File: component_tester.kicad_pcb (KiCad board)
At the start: 2 copper layers, 93 x 34 mm, 77 parts, among them IC1 ATMEGA16U2, IC2 ATMEGA328P-A, P1 USB_OTG, P10 BO_PC5, P11 ICSP_prog_328p, P12 BO_PD2, P13 BO_PD3, P14 BO_PD4, P15 BO_PD5, P16 BO_PD6, P17 CONN_01X01, P18 Device Under Test, P2 BATTERY_CONNECTOR, P3 Voltage_for_zener, P4 ICSP_prog_16u2, P5 BO_PC7, P6 BO_PD0, P7 BO_PD1, P8 BO_PC4, P9 BO_PC6, Q1 TRANSISTOR_NPN_2N2222_KSP222A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, SW1 ON-OFF switch, SW2 DO_MEASUREMENT, SW3 CONNECT_CAP, U1 NCP1117ST50T3G, U2 XF2L-2625-1A, U3 LT1004, U4 CDSOT23-SRV05-4, Y1 8MHz, Y2 16MHz

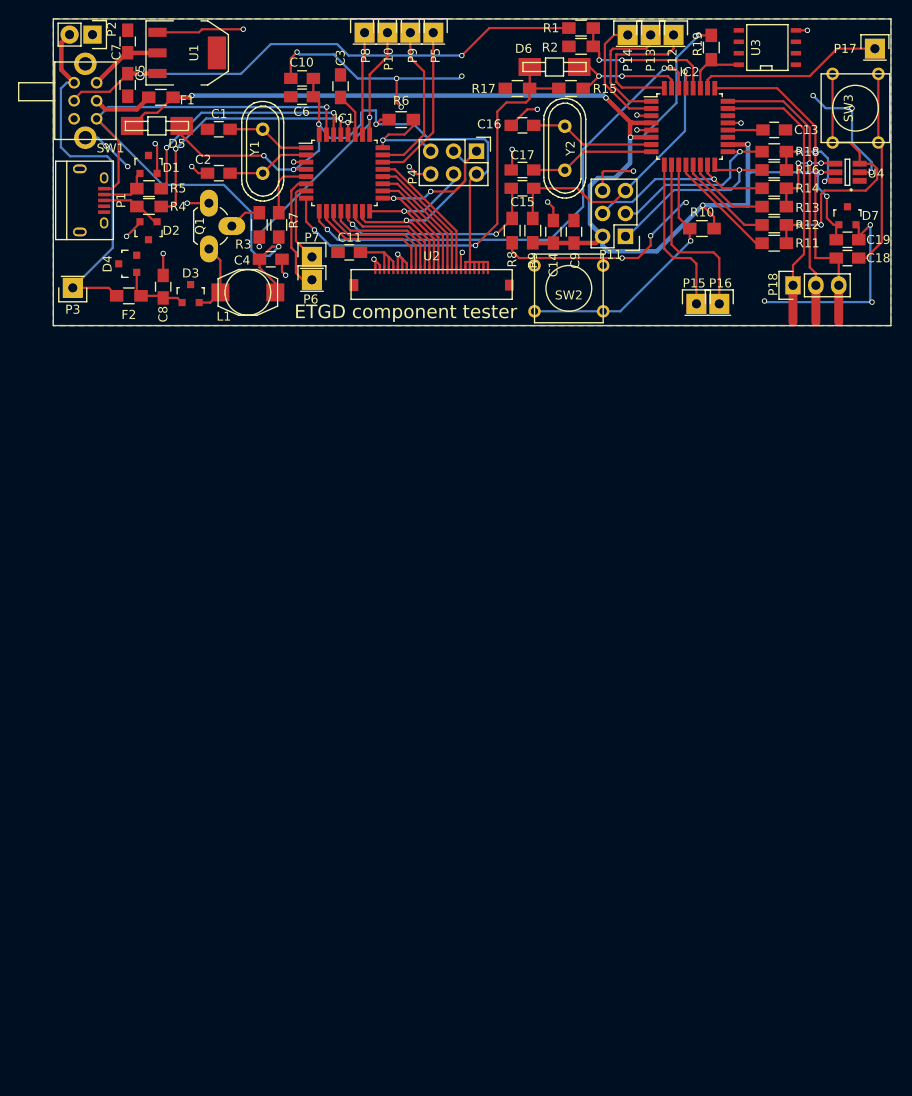
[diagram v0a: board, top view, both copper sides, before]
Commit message: Updated schematic. New PCB layout.
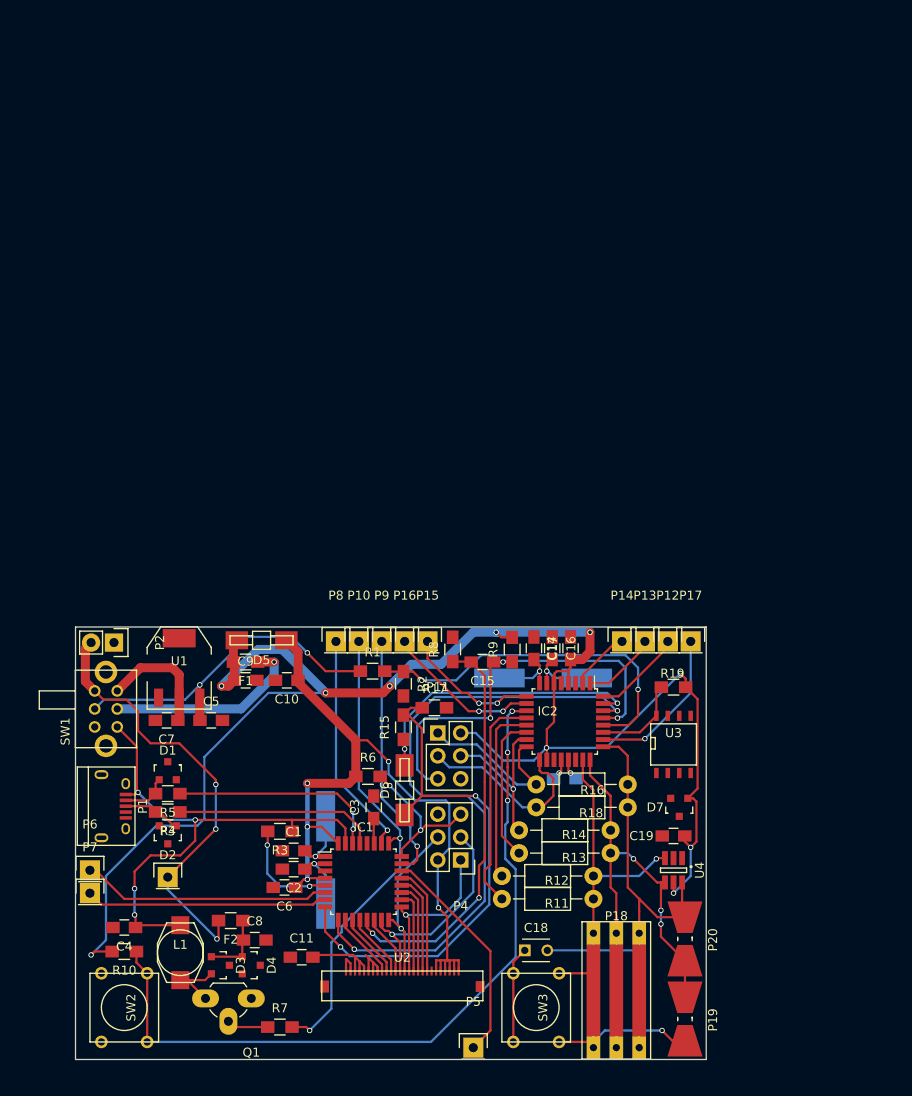
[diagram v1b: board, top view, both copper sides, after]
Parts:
- added P19: DUT_SMD_1_2, Resistors_Universal:Resistor_SMDuniversal_0805to2512_HandSoldering, F.Cu at (167.6, 143.5)
- added P20: DUT_SMD_2_3, Resistors_Universal:Resistor_SMDuniversal_0805to2512_HandSoldering, F.Cu at (167.6, 134.6)
- C13: moved to B.Cu
- C18: footprint Capacitors_SMD:C_0805_HandSoldering -> Capacitors_ThroughHole:C_Disc_D3_P2.5
- P18: footprint Pin_Headers:Pin_Header_Straight_1x03 -> drawn_by_jpmeijers:CONN_DUT
- R11, R12, R13, R14, R16, R18: footprint Resistors_SMD:R_0805_HandSoldering -> Resistors_ThroughHole:Resistor_Horizontal_RM10mm
- Y1, Y2: footprint Crystals:Crystal_HC49-U_Vertical -> Crystals:Crystal_HC49-SD_SMD; moved to B.Cu
- moved P5 112.7 mm to (144.1, 146.7)
- moved SW3 105.9 mm to (151.1, 142.2), turned to 270 degrees
- moved R10 102.7 mm to (105.4, 136.0), turned to 180 degrees
- moved SW2 93.8 mm to (105.4, 142.2), turned to 270 degrees
- moved R7 89.1 mm to (122.7, 144.4), turned to 0 degrees
- moved Q1 88.4 mm to (119.5, 141.2), turned to 180 degrees
- moved C6 87.8 mm to (123.2, 128.9)
- moved C18 84.8 mm to (149.9, 135.9), turned to 0 degrees
- moved D6 82.0 mm to (136.5, 118.1), turned to 270 degrees
- moved C1 80.5 mm to (124.2, 124.8)
- moved C3 80.1 mm to (133.1, 120.0)
- moved U4 79.8 mm to (166.4, 127.0), turned to 270 degrees
- moved D4 79.1 mm to (119.5, 137.5), turned to 270 degrees
- moved Y1 79.0 mm to (127.8, 125.9)
- moved IC1 78.7 mm to (132.0, 128.3)
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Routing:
- net GND: track 156.2 -> 10.3 mm, vias 36 -> 1
- net Net-(IC2-Pad11): track 29.7 -> 85.0 mm, vias 1 -> 3
- net 5Volt_328: track 154.2 -> 183.4 mm, vias 8 -> 10
- net /Battery_measure: track 17.0 -> 40.2 mm
- net Batt_Switch: track 61.5 -> 38.3 mm
- net Net-(C15-Pad2): track 24.2 -> 45.1 mm
- net /CHARGER_SWITCHING: track 32.7 -> 52.8 mm
- net UART_16u_TO_328: track 55.4 -> 73.4 mm
- net Net-(D6-Pad2): track 14.1 -> 32.0 mm
- net Net-(IC1-Pad7): track 9.07 -> 26.9 mm
- net /USB_Vcc: track 76.7 -> 59.1 mm, vias 2 -> 4
- net Net-(F1-Pad1): track 6.73 -> 22.3 mm, vias 0 -> 1
- net Net-(IC1-Pad6): track 13.4 -> 27.7 mm
- net /RESET_328: track 32.2 -> 46.4 mm, vias 1 -> 3
- net Net-(IC1-Pad26): track 11.4 -> 25.1 mm, vias 0 -> 1
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- removed copper zone on B.Cu, net GND
- removed copper zone on F.Cu, net GND
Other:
- board size 93 x 34 mm -> 70 x 48 mm
- rule pad_to_mask_clearance: 0.2 -> 0
- board text removed: "2016-06-17"
- board text removed: "ETGD component tester"

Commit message: Version 3 of the PCB
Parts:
- added C12: 1n, Capacitors_SMD:C_0805_HandSoldering, B.Cu at (150.7, 124.6)
- added P21: ICSP_prog_328_4, Pin_Headers:Pin_Header_Straight_1x01, F.Cu at (142.2, 119.4)
- added P22: ICSP_prog_328_5, Pin_Headers:Pin_Header_Straight_1x01, F.Cu at (160.0, 116.8)
- added P23: CONN_01X01, Pin_Headers:Pin_Header_Straight_1x01, F.Cu at (161.3, 120.3)
- added P24: Device Under Test, drawn_by_jpmeijers:CONN_DUT, F.Cu at (149.8, 135.2)
- added P25: CONN_01X03, drawn_by_jpmeijers:CONN_DUT_SMD, F.Cu at (165.9, 143.8)
- C1, C16, C19, C2, C3, C5, C6, C7, R10, U4: moved to B.Cu
- C13: value 1n -> 100n
- C15: value 100n -> 22pF; moved to B.Cu
- C17: value 22pF -> 22nF high quality; footprint Capacitors_SMD:C_0805_HandSoldering -> Capacitors_ThroughHole:C_Disc_D3_P2.5
- C18: value 22nF high quality -> 100n; footprint Capacitors_ThroughHole:C_Disc_D3_P2.5 -> Capacitors_SMD:C_0805_HandSoldering
- P10: value BO_PC5 -> ICSP_prog_16u2_4
- P11: value ICSP_prog_328p -> BO_PC6; footprint Pin_Headers:Pin_Header_Straight_2x03 -> Pin_Headers:Pin_Header_Straight_1x01
- P12: value BO_PD2 -> ICSP_prog_16u2_5
- P13: value BO_PD3 -> BO_PC5
- P14: value BO_PD4 -> BO_PD2
- P15: value BO_PD5 -> BO_PD3
- P16: value BO_PD6 -> BO_PD4
- P17: value CONN_01X01 -> BO_PD5
- P18: value Device Under Test -> BO_PD6; footprint drawn_by_jpmeijers:CONN_DUT -> Pin_Headers:Pin_Header_Straight_1x01
- P19: value DUT_SMD_1_2 -> ICSP_prog_328_1; footprint Resistors_Universal:Resistor_SMDuniversal_0805to2512_HandSoldering -> Pin_Headers:Pin_Header_Straight_1x01
- P20: value DUT_SMD_2_3 -> ICSP_prog_328_3; footprint Resistors_Universal:Resistor_SMDuniversal_0805to2512_HandSoldering -> Pin_Headers:Pin_Header_Straight_1x01
- P4: value ICSP_prog_16u2 -> BO_PC7; footprint Pin_Headers:Pin_Header_Straight_2x03 -> Pin_Headers:Pin_Header_Straight_1x01
- P5: value BO_PC7 -> ICSP_prog_16u2_1
- P9: value BO_PC6 -> ICSP_prog_16u2_3
- Q1: footprint TO_SOT_Packages_THT:TO-92_Rugged -> TO_SOT_Packages_THT:TO-92_Inline_Narrow_Oval
- R1: value 100k -> R
- R11, R12, R13, R14, R16, R18: footprint Resistors_ThroughHole:Resistor_Horizontal_RM10mm -> Resistors_SMD:R_0805_HandSoldering
- R2: value 33k -> 22
- R3: value R -> 22
- R4: value 22 -> 10k
- R5: value 22 -> 100k
- R6: value 10k -> 33k
- U2: footprint drawn_by_jpmeijers:XF2L-2625-1A -> drawn_by_jpmeijers:CONN_FPC_FFC_0.5mm_26PIN_DRAWER_BOTTOM
- Y1, Y2: footprint Crystals:Crystal_HC49-SD_SMD -> Crystals:Crystal_HC49-U_Vertical; moved to F.Cu
- moved R10 47.0 mm to (148.0, 116.1), turned to 0 degrees
- moved C17 45.2 mm to (140.7, 146.4), turned to 0 degrees
- moved P10 36.3 mm to (135.3, 137.7)
- moved P9 36.1 mm to (132.7, 137.7)
- moved P19 33.3 mm to (142.2, 121.9), turned to 0 degrees
- moved P12 31.9 mm to (135.6, 112.3)
- moved R2 31.7 mm to (109.9, 123.6), turned to 180 degrees
- moved F2 31.7 mm to (102.4, 104.6)
- moved P13 31.3 mm to (132.8, 109.3)
- moved R5 31.1 mm to (138.3, 105.1), turned to 0 degrees
- moved R15 30.4 mm to (166.8, 112.9)
- moved D6 29.1 mm to (165.0, 112.0), turned to 90 degrees
- moved P17 28.4 mm to (142.2, 113.0)
- moved P20 26.9 mm to (142.2, 126.0), turned to 0 degrees
- moved P18 25.6 mm to (142.2, 115.6)
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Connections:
- C13 pad 1: Net-(C13-Pad1) -> 5Volt_328
- C14 pad 1: 5Volt_328 -> /RESET_328
- C14 pad 2: GND -> Net-(C14-Pad2)
- C15 pad 1: /RESET_328 -> GND
- C17 pad 1: GND -> Net-(C17-Pad1)
- C17 pad 2: Net-(C17-Pad2) -> /DUT3
- C18 pad 1: Net-(C18-Pad1) -> 5Volt_328
- C18 pad 2: /DUT3 -> GND
- C8 pad 1: Net-(C8-Pad1) -> Battery_fused
- D3 pad 1: Net-(C8-Pad1) -> Battery_fused
- D4 pad 1: Net-(C8-Pad1) -> Battery_fused
- F1 pad 2: 5Volt_328 -> /USB_Vcc
- F2 pad 1: Net-(C8-Pad1) -> Battery_input
- F2 pad 2: Battery_input -> Battery_fused
- IC1 pad 13: Net-(C15-Pad2) -> Net-(C14-Pad2)
- IC2 pad 15: Net-(IC2-Pad15) -> /328_MOSI
- IC2 pad 16: Net-(IC2-Pad16) -> /328_MISO
- IC2 pad 17: Net-(IC2-Pad17) -> /328_SCK
- IC2 pad 20: Net-(C13-Pad1) -> Net-(C12-Pad1)
- IC2 pad 7: Net-(C16-Pad2) -> Net-(C15-Pad2)
- IC2 pad 8: Net-(C17-Pad2) -> Net-(C16-Pad2)
- P1 pad 1: /USB_Vcc -> Net-(F1-Pad1)
- P10 pad 1: /CHARGER_SWITCHING -> /LCD_DATA_B2
- P11 pad 1: Net-(IC2-Pad16) -> Net-(IC1-Pad23)
- P12 pad 1: Net-(IC2-Pad32) -> /RESET_16u
- P13 pad 1: Net-(IC2-Pad1) -> /CHARGER_SWITCHING
- P14 pad 1: Net-(IC2-Pad2) -> Net-(IC2-Pad32)
- P15 pad 1: Net-(IC2-Pad9) -> Net-(IC2-Pad1)
- P16 pad 1: Net-(IC2-Pad10) -> Net-(IC2-Pad2)
- P17 pad 1: Net-(IC2-Pad26) -> Net-(IC2-Pad9)
- P18 pad 1: /DUT1 -> Net-(IC2-Pad10)
- P19 pad 1: /DUT2 -> /328_MISO
- P20 pad 1: /DUT3 -> /328_SCK
- P3 pad 1: Battery_input -> Battery_fused
- P4 pad 1: /LCD_DATA_B3 -> Net-(IC1-Pad22)
- P5 pad 1: Net-(IC1-Pad22) -> /LCD_DATA_B3
- P9 pad 1: Net-(IC1-Pad23) -> /LCD_DATA_B1
- R1 pad 1: Batt_Switch -> /USB_Vcc
- R1 pad 2: /Battery_measure -> /CHARGER_VOLTAGE_SENSE
- R14 pad 2: Net-(IC2-Pad15) -> /328_MOSI
- R16 pad 2: Net-(IC2-Pad16) -> /328_MISO
- R18 pad 2: Net-(IC2-Pad17) -> /328_SCK
- R2 pad 1: /Battery_measure -> Net-(IC1-Pad29)
- R2 pad 2: GND -> /USB_D+
- R3 pad 1: /USB_Vcc -> Net-(IC1-Pad30)
- R3 pad 2: /CHARGER_VOLTAGE_SENSE -> /USB_D-
- R4 pad 1: Net-(IC1-Pad29) -> 3Volt_16u
- R4 pad 2: /USB_D+ -> /RESET_16u
- R5 pad 1: Net-(IC1-Pad30) -> Batt_Switch
- R5 pad 2: /USB_D- -> /Battery_measure
- R6 pad 1: 3Volt_16u -> /Battery_measure
- R6 pad 2: /RESET_16u -> GND
- R8 pad 1: Net-(C15-Pad2) -> Net-(C14-Pad2)
- SW1 pad 1: Net-(F1-Pad1) -> 5Volt_328
- SW1 pad 5: Battery_input -> Battery_fused
- SW3 pad 2: Net-(C18-Pad1) -> Net-(C17-Pad1)
- Y2 pad 1: Net-(C16-Pad2) -> Net-(C15-Pad2)
- Y2 pad 2: Net-(C17-Pad2) -> Net-(C16-Pad2)
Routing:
- net Battery_fused: track 0.00 -> 47.4 mm
- net Battery_input: track 49.1 -> 3.06 mm, vias 3 -> 0
- net Net-(C14-Pad2): track 0.00 -> 43.9 mm, vias 0 -> 2
- net Net-(C15-Pad2): track 45.1 -> 6.25 mm, vias 2 -> 0
- net /RESET_328: track 46.4 -> 10.9 mm, vias 3 -> 0
- net UART_16u_TO_328: track 73.4 -> 41.9 mm
- net Net-(IC1-Pad23): track 27.8 -> 3.94 mm, vias 1 -> 0
- net /Reference_voltage: track 10.1 -> 32.8 mm
- net Net-(IC1-Pad22): track 25.1 -> 2.77 mm
- net /CHARGER_SWITCHING: track 52.8 -> 31.3 mm
- net Net-(IC1-Pad6): track 27.7 -> 6.36 mm
- net Net-(IC2-Pad17): track 20.7 -> 0.00 mm
- net Net-(D6-Pad2): track 32.0 -> 11.6 mm, vias 2 -> 0
- net Net-(IC2-Pad16): track 18.9 -> 0.00 mm
- net Net-(IC2-Pad15): track 18.8 -> 0.00 mm, vias 1 -> 0
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- added copper zone on B.Cu, net GND
- added copper zone on F.Cu, net GND

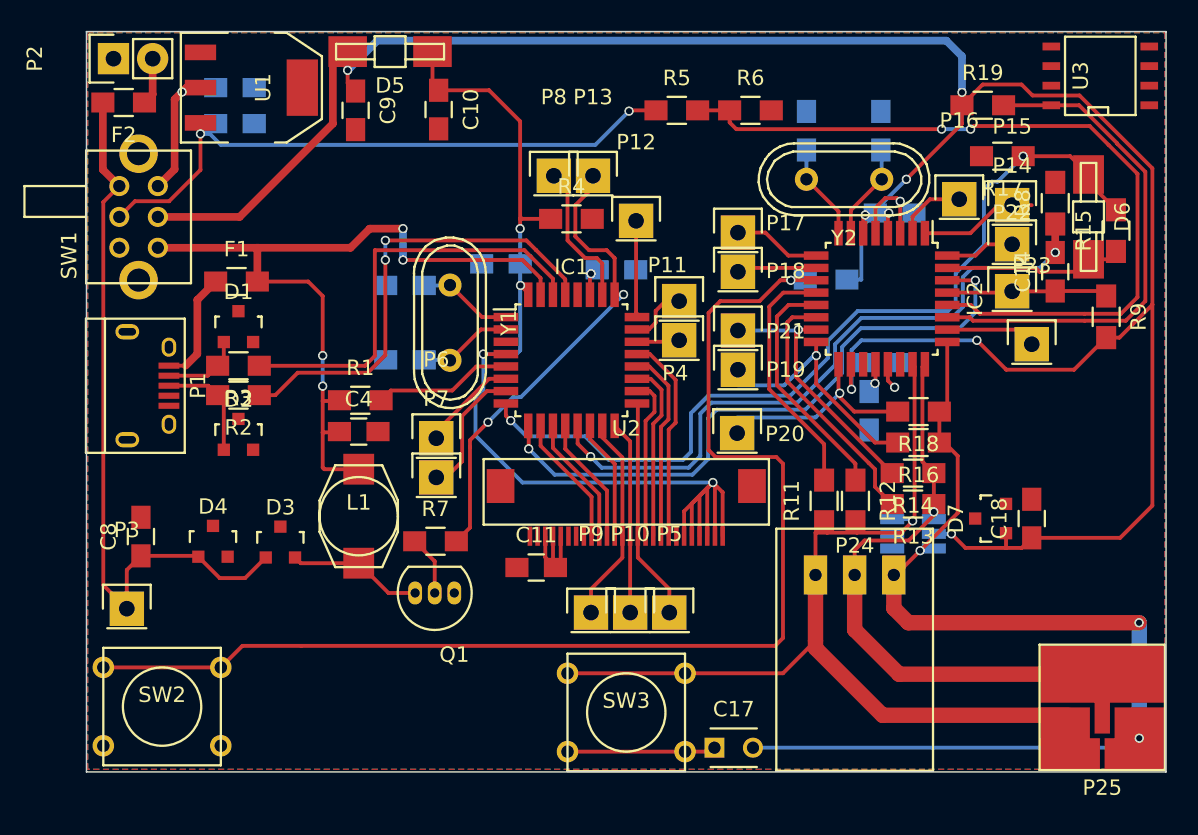
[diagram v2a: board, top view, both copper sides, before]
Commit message: Resonator Capacitor closer. A lot of GND vias.
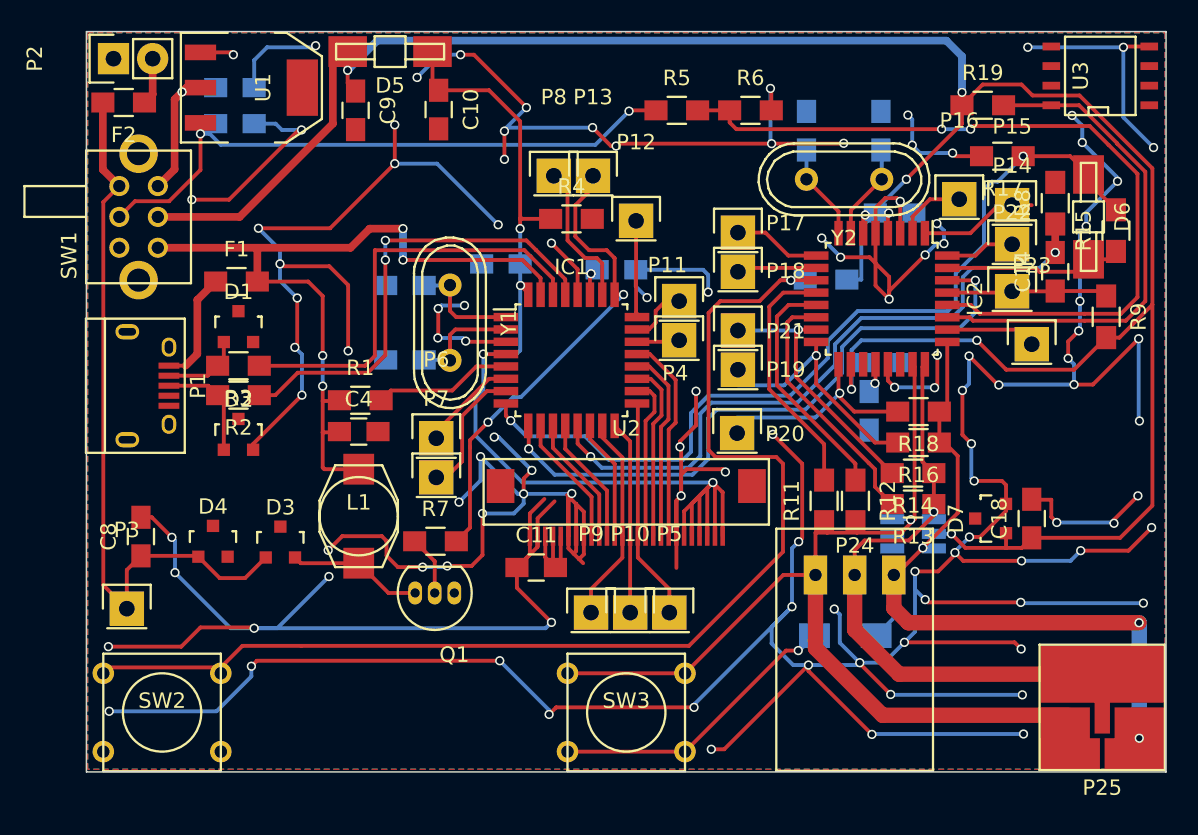
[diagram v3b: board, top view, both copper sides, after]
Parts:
- C17: footprint Capacitors_ThroughHole:C_Disc_D3_P2.5 -> Capacitors_SMD:C_1206_HandSoldering; moved to B.Cu
- moved C17 11.2 mm to (149.2, 139.2)
- moved SW2 0.38 mm to (104.9, 144.1)
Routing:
- net GND: track 8.54 -> 540.1 mm, vias 2 -> 111
- net /DUT3: track 70.7 -> 51.5 mm
- net Net-(C17-Pad1): track 9.63 -> 19.1 mm, vias 0 -> 1
- net Net-(IC2-Pad11): track 79.1 -> 75.8 mm
- net /DUT1: track 64.1 -> 65.8 mm
- net Net-(C1-Pad2): track 6.17 -> 7.15 mm
- net Net-(C2-Pad1): track 6.14 -> 7.10 mm

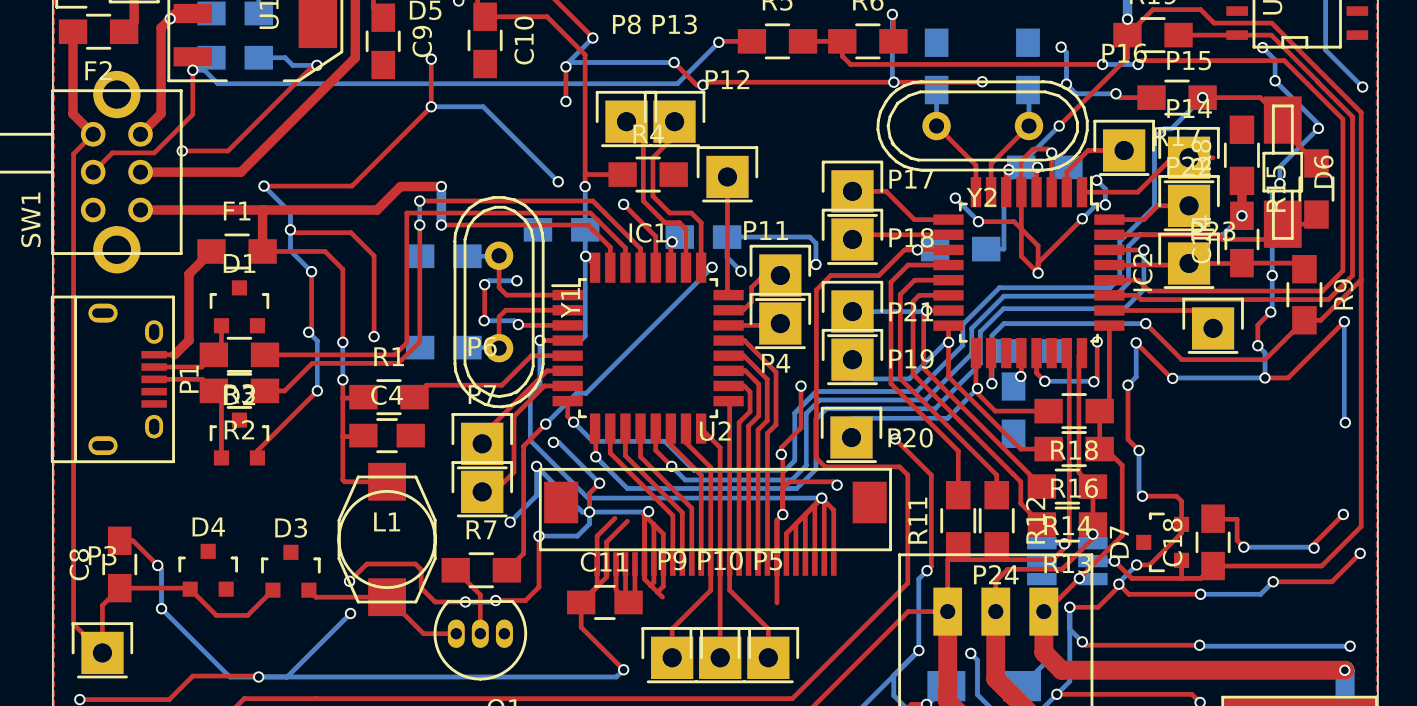
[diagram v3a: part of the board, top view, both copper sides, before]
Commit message: Added extra vias. Add cap on LCD power.
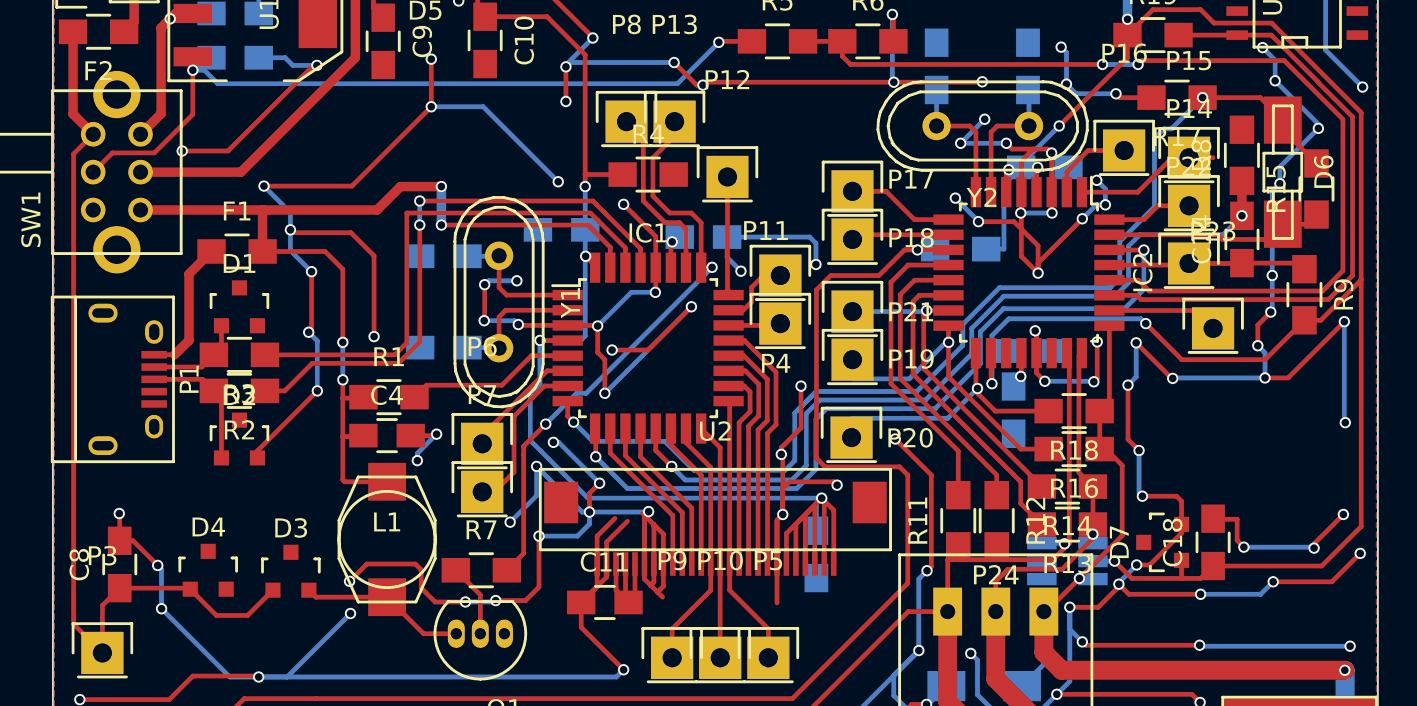
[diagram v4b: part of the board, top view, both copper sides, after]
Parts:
- added C20: 100n, Capacitors_SMD:C_0805_HandSoldering, B.Cu at (140.3, 132.2)
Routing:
- net GND: track 540.1 -> 576.6 mm, vias 111 -> 125
- net 3Volt_16u: track 76.5 -> 78.3 mm
- net Net-(C16-Pad2): track 6.26 -> 7.29 mm
- net Net-(C15-Pad2): track 6.25 -> 7.23 mm
